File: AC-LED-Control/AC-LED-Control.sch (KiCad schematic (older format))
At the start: 1 part

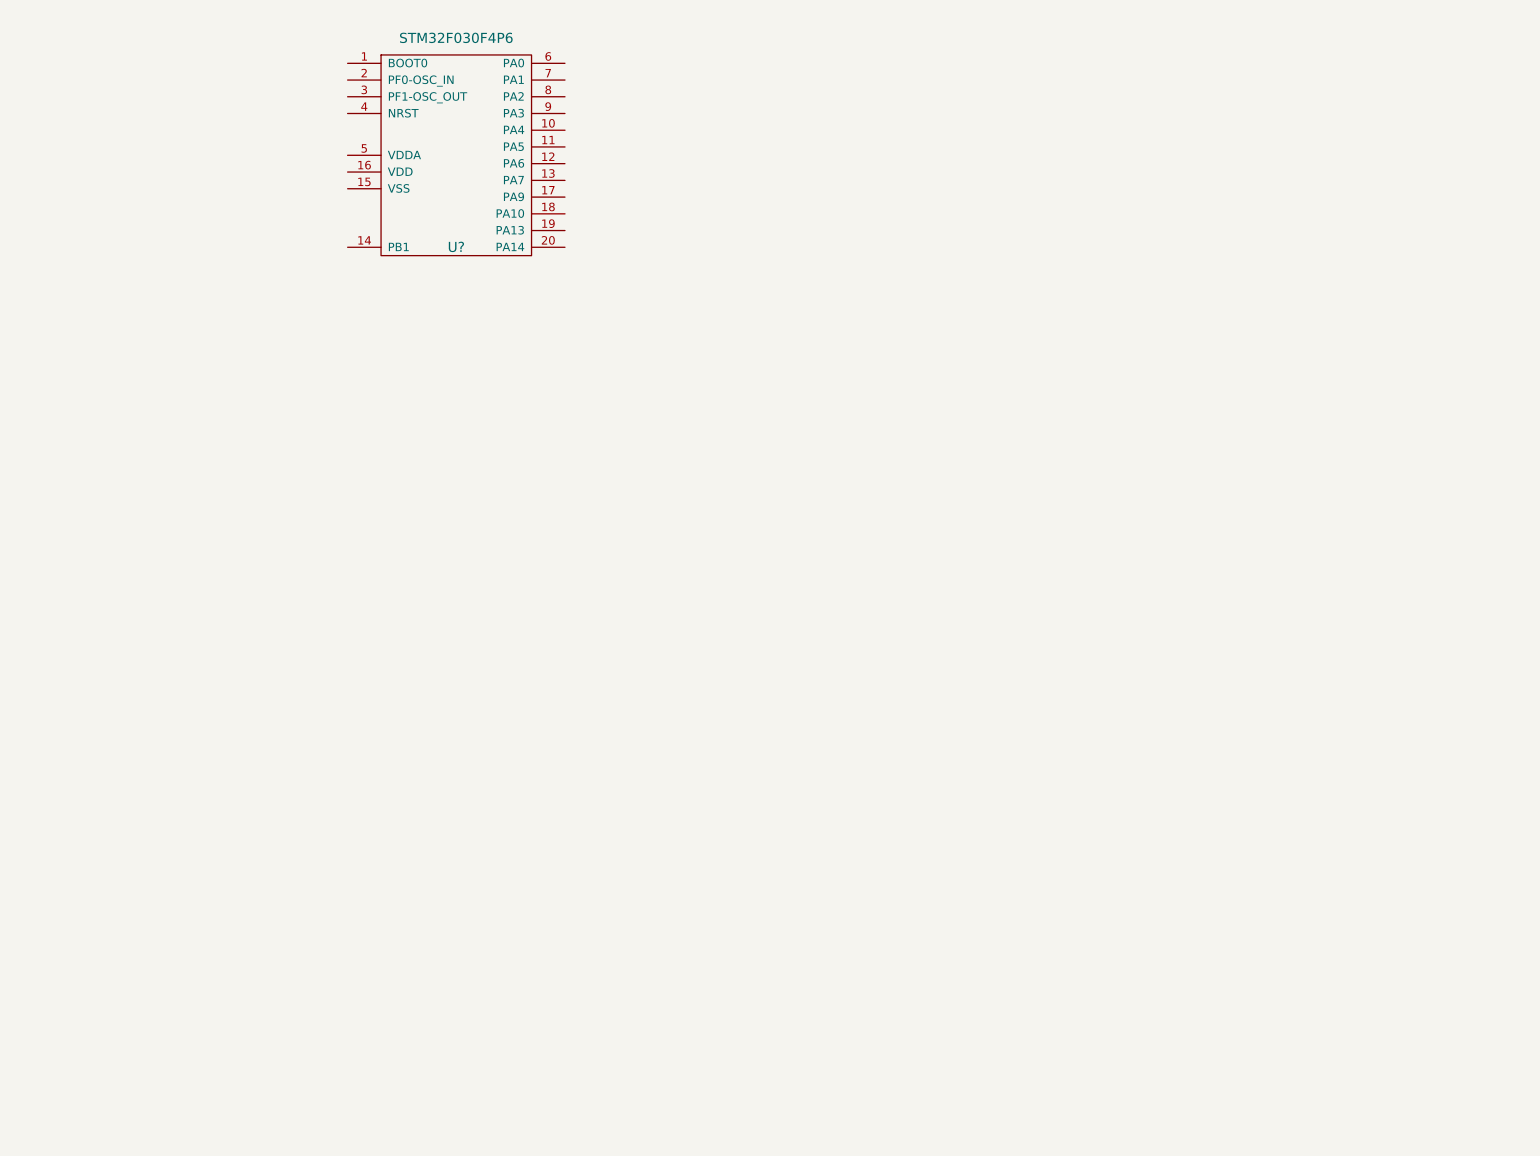
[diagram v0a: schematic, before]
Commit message: Added notes.md and started digital stuff.
- Added notes.md
- Added bypass caps to STM32
- Added I2C stuff
- Added 2 SN74HC595's and various nets
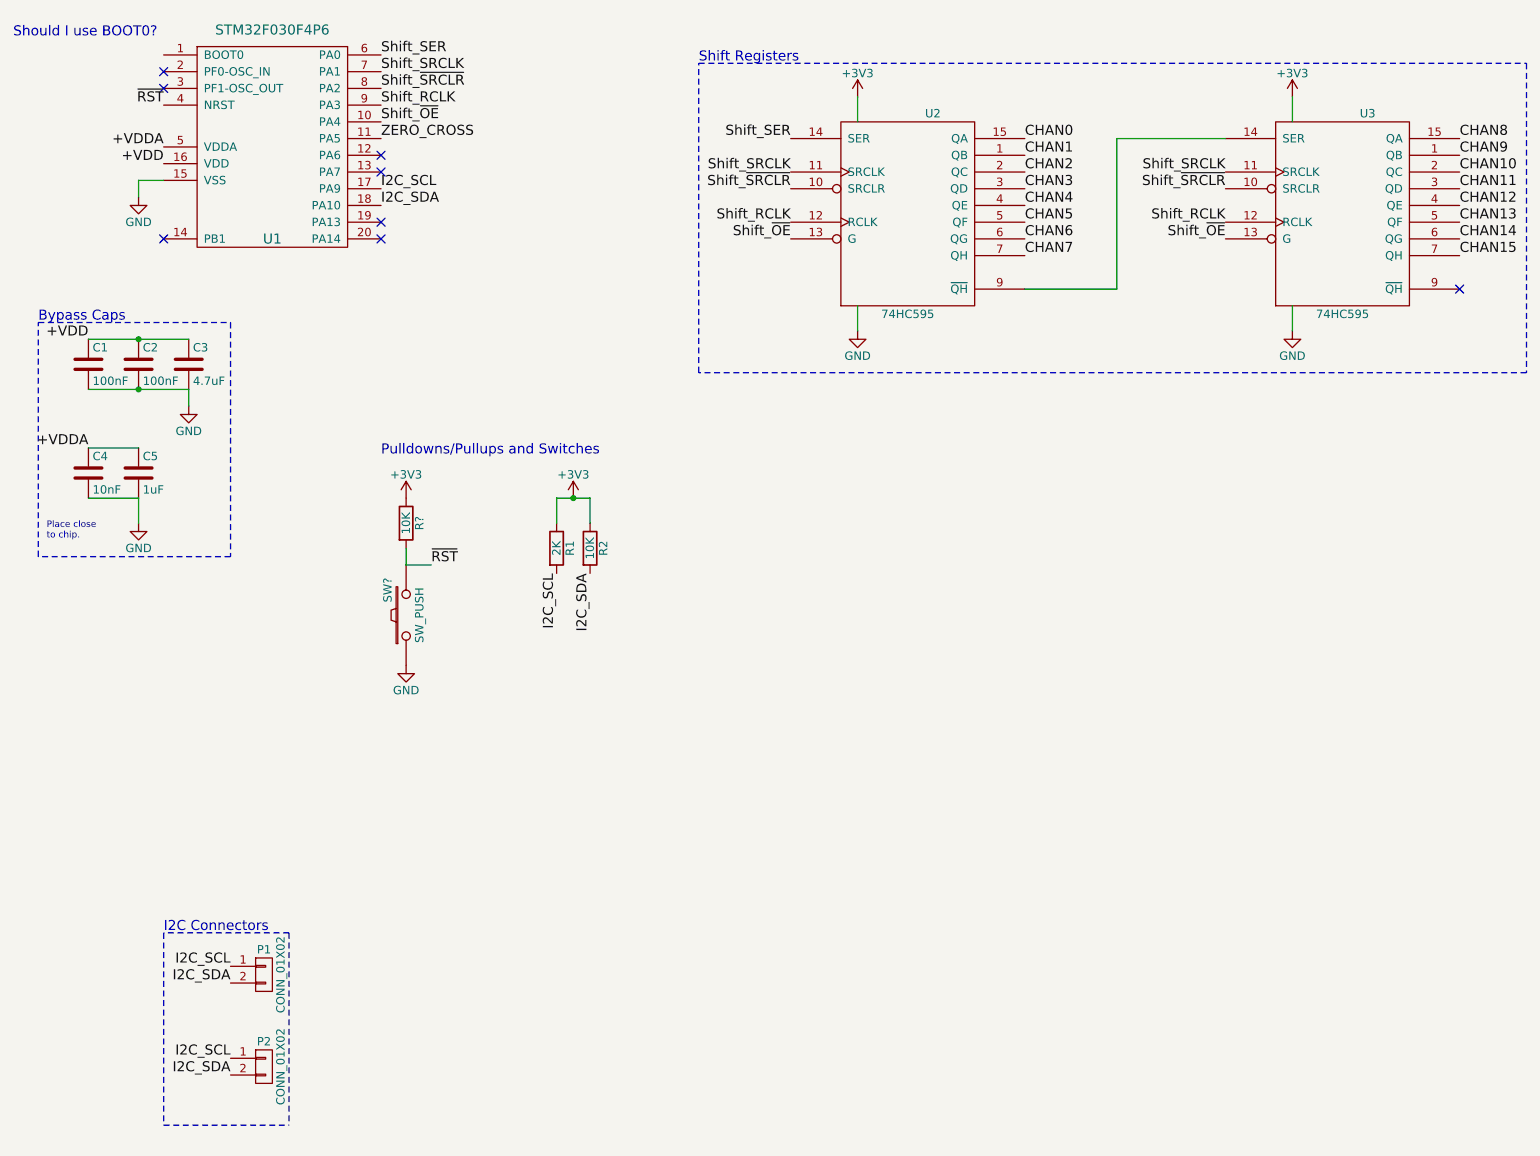
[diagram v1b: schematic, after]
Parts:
- added C1, C2: 100nF, symbol C
- added C3: 4.7uF, symbol C
- added C4: 10nF, symbol C
- added C5: 1uF, symbol C
- added P1, P2: CONN_01X02, symbol CONN_01X02
- added R1: 2K, symbol R
- added R2, R?: 10K, symbol R
- added SW?: SW_PUSH, symbol SW_PUSH
- added U2, U3: 74HC595, symbol 74HC595
- gave numbers to parts that had none: 1
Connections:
- net Shift_~OE: now reaches U1.10 (PA4)
- net Shift_~OE: now also U2.13 (G), U3.13 (G)
- net ZERO_CROSS: now reaches U1.11 (PA5)
- net GND: now reaches U1.15 (VSS)
- net GND: now also C1.2, C2.2, C3.2, C4.2, C5.2, SW?.1, U2.8 (GND), U3.8 (GND)
- net +VDD: now reaches U1.16 (VDD)
- net +VDD: now also C1.1, C2.1, C3.1
- net I2C_SCL: now reaches U1.17 (PA9)
- net I2C_SCL: now also P1.1 (P1), P2.1 (P1), R1.2
- net I2C_SDA: now reaches U1.18 (PA10)
- net I2C_SDA: now also P1.2 (P2), P2.2 (P2), R2.2
- net ~RST: now reaches U1.4 (NRST)
- net ~RST: now also R?.2, SW?.2
- net +VDDA: now reaches U1.5 (VDDA)
- net +VDDA: now also C4.1, C5.1
- net Shift_SER: now reaches U1.6 (PA0)
- net Shift_SER: now also U2.14 (SER)
- net Shift_SRCLK: now reaches U1.7 (PA1)
- net Shift_SRCLK: now also U2.11 (SRCLK), U3.11 (SRCLK)
- net Shift_~SRCLR: now reaches U1.8 (PA2)
- net Shift_~SRCLR: now also U2.10 (SRCLR), U3.10 (SRCLR)
- net Shift_RCLK: now reaches U1.9 (PA3)
- net Shift_RCLK: now also U2.12 (RCLK), U3.12 (RCLK)
- new net: U2.9 (~QH), U3.14 (SER)
- new net +3V3: R1.1, R2.1, R?.1, U2.16 (VCC), U3.16 (VCC)
- new net CHAN0: U2.15 (QA)
- new net CHAN1: U2.1 (QB)
- new net CHAN10: U3.2 (QC)
- new net CHAN11: U3.3 (QD)
- new net CHAN12: U3.4 (QE)
- new net CHAN13: U3.5 (QF)
- new net CHAN14: U3.6 (QG)
- new net CHAN15: U3.7 (QH)
- new net CHAN2: U2.2 (QC)
- new net CHAN3: U2.3 (QD)
- new net CHAN4: U2.4 (QE)
- new net CHAN5: U2.5 (QF)
- new net CHAN6: U2.6 (QG)
- new net CHAN7: U2.7 (QH)
- new net CHAN8: U3.15 (QA)
- new net CHAN9: U3.1 (QB)
- no-connect marks 0 -> 8
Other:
- note added: "Bypass Caps\n"
- note added: "I2C Connectors\n"
- note added: "Place close\nto chip."
- note added: "Pulldowns/Pullups and Switches"
- note added: "Shift Registers"
- note added: "Should I use BOOT0?"
- moved on the sheet: U1

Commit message: Pulled BOOT0 to GND
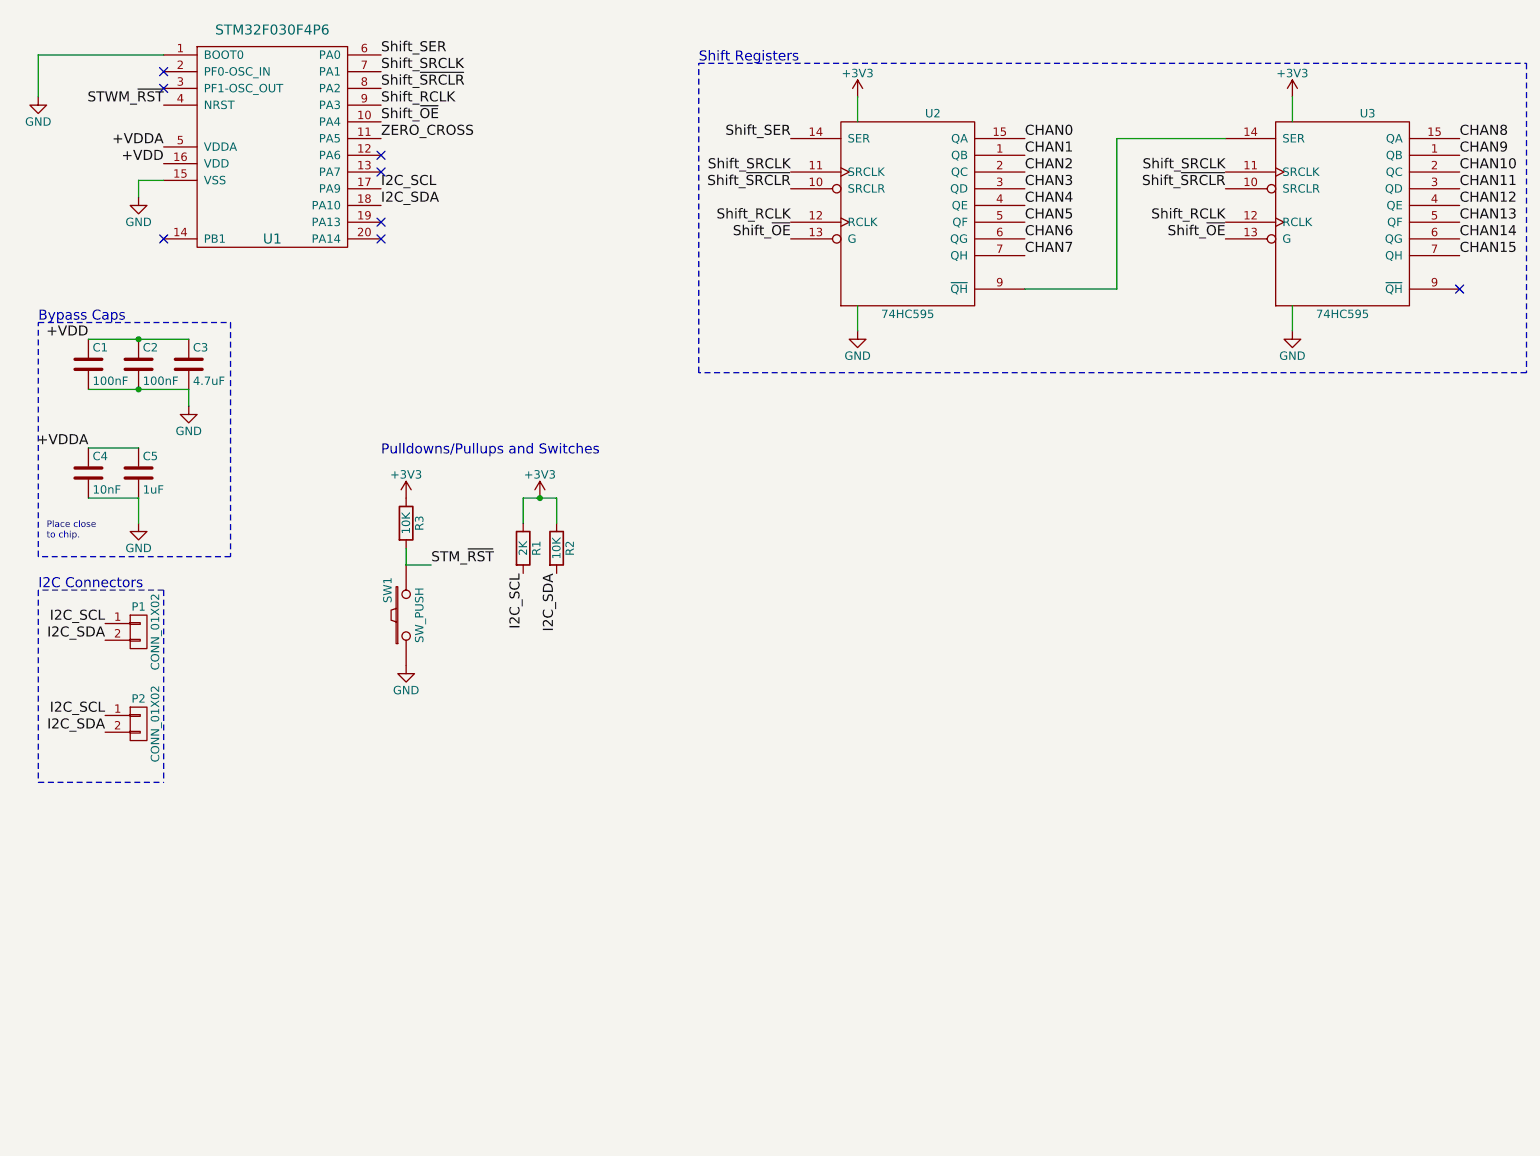
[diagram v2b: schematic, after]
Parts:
- gave numbers to parts that had none: 2
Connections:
- net GND: now also U1.1 (BOOT0)
- net ~RST renamed STM_~RST
- net STM_~RST: no longer U1.4 (NRST)
- new net STWM_~RST: U1.4 (NRST)
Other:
- note removed: "Should I use BOOT0?"
- moved on the sheet: P1, P2, R1, R2
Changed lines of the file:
@@
 L CONN_01X02 P1
 U 1 1 5B453C99
-P 2150 6500
-F 0 "P1" H 2150 6650 50  0000 C CNN
-F 1 "CONN_01X02" V 2250 6500 50  0000 C CNN
-F 2 "" H 2150 6500 50  0000 C CNN
-F 3 "" H 2150 6500 50  0000 C CNN
-	1    2150 6500
+P 1400 4450
+F 0 "P1" H 1400 4600 50  0000 C CNN
+F 1 "CONN_01X02" V 1500 4450 50  0000 C CNN
+F 2 "" H 1400 4450 50  0000 C CNN
+F 3 "" H 1400 4450 50  0000 C CNN
+	1    1400 4450
 	1    0    0    -1
 $EndComp
@@
 L CONN_01X02 P2
 U 1 1 5B453DC6
-P 2150 7050
-F 0 "P2" H 2150 7200 50  0000 C CNN
-F 1 "CONN_01X02" V 2250 7050 50  0000 C CNN
-F 2 "" H 2150 7050 50  0000 C CNN
-F 3 "" H 2150 7050 50  0000 C CNN
-	1    2150 7050
-	1    0    0    -1
-$EndComp
-Text Label 1950 6450 2    60   ~ 0
+P 1400 5000
+F 0 "P2" H 1400 5150 50  0000 C CNN
+F 1 "CONN_01X02" V 1500 5000 50  0000 C CNN
+F 2 "" H 1400 5000 50  0000 C CNN
+F 3 "" H 1400 5000 50  0000 C CNN
+	1    1400 5000
+	1    0    0    -1
+$EndComp
+Text Label 1200 4400 2    60   ~ 0
 I2C_SCL
-Text Label 1950 6550 2    60   ~ 0
+Text Label 1200 4500 2    60   ~ 0
 I2C_SDA
-Text Label 1950 7000 2    60   ~ 0
+Text Label 1200 4950 2    60   ~ 0
 I2C_SCL
-Text Label 1950 7100 2    60   ~ 0
+Text Label 1200 5050 2    60   ~ 0
 I2C_SDA
 Wire Notes Line
-	2300 6250 2300 7400
-Text Notes 1550 6250 0    60   ~ 0
+	1550 4200 1550 5350
+Text Notes 800  4200 0    60   ~ 0
 I2C Connectors\n
+Text Label 3700 4100 3    60   ~ 0
+I2C_SCL
 Text Label 3900 4100 3    60   ~ 0
-I2C_SCL
-Text Label 4100 4100 3    60   ~ 0
 I2C_SDA
 $Comp
 L R R1
 U 1 1 5B453F03
+P 3700 3950
+F 0 "R1" V 3780 3950 50  0000 C CNN
+F 1 "2K" V 3700 3950 50  0000 C CNN
+F 2 "" V 3630 3950 50  0000 C CNN
+F 3 "" H 3700 3950 50  0000 C CNN
+	1    3700 3950
+	1    0    0    -1
+$EndComp
+$Comp
+L R R2
+U 1 1 5B453F30
 P 3900 3950
-F 0 "R1" V 3980 3950 50  0000 C CNN
-F 1 "2K" V 3900 3950 50  0000 C CNN
+F 0 "R2" V 3980 3950 50  0000 C CNN
+F 1 "10K" V 3900 3950 50  0000 C CNN
 F 2 "" V 3830 3950 50  0000 C CNN
 F 3 "" H 3900 3950 50  0000 C CNN
@@
 $EndComp
 $Comp
-L R R2
-U 1 1 5B453F30
-P 4100 3950
-F 0 "R2" V 4180 3950 50  0000 C CNN
-F 1 "10K" V 4100 3950 50  0000 C CNN
-F 2 "" V 4030 3950 50  0000 C CNN
-F 3 "" H 4100 3950 50  0000 C CNN
-	1    4100 3950
-	1    0    0    -1
-$EndComp
-$Comp
-L +3V3 #PWR4
+L +3V3 #PWR01
 U 1 1 5B45401C
-P 4000 3650
-F 0 "#PWR4" H 4000 3500 50  0001 C CNN
-F 1 "+3V3" H 4000 3790 50  0000 C CNN
-F 2 "" H 4000 3650 50  0000 C CNN
-F 3 "" H 4000 3650 50  0000 C CNN
-	1    4000 3650
-	1    0    0    -1
-$EndComp
-Wire Wire Line
-	3900 3800 3900 3650
-Wire Wire Line
-	3900 3650 4100 3650
-Wire Wire Line
-	4100 3650 4100 3800
-Connection ~ 4000 3650
+P 3800 3650
+F 0 "#PWR01" H 3800 3500 50  0001 C CNN
+F 1 "+3V3" H 3800 3790 50  0000 C CNN
+F 2 "" H 3800 3650 50  0000 C CNN
+F 3 "" H 3800 3650 50  0000 C CNN
+	1    3800 3650
+	1    0    0    -1
+$EndComp
+Wire Wire Line
+	3700 3800 3700 3650
+Wire Wire Line
+	3700 3650 3900 3650
+Wire Wire Line
+	3900 3650 3900 3800
+Connection ~ 3800 3650
 Text Label 1550 1650 2    60   ~ 0
 +VDD
@@
 	1400 1750 1400 1850
 $Comp
-L GND #PWR1
+L GND #PWR02
 U 1 1 5B454DB5
 P 1400 1850
-F 0 "#PWR1" H 1400 1600 50  0001 C CNN
+F 0 "#PWR02" H 1400 1600 50  0001 C CNN
 F 1 "GND" H 1400 1700 50  0000 C CNN
 F 2 "" H 1400 1850 50  0000 C CNN
@@
 $EndComp
 $Comp
-L GND #PWR2
+L GND #PWR03
 U 1 1 5B454DF7
 P 1700 3100
-F 0 "#PWR2" H 1700 2850 50  0001 C CNN
+F 0 "#PWR03" H 1700 2850 50  0001 C CNN
 F 1 "GND" H 1700 2950 50  0000 C CNN
 F 2 "" H 1700 3100 50  0000 C CNN
@@
 $EndComp
 $Comp
-L GND #PWR3
+L GND #PWR04
 U 1 1 5B454F8F
 P 1400 3800
-F 0 "#PWR3" H 1400 3550 50  0001 C CNN
+F 0 "#PWR04" H 1400 3550 50  0001 C CNN
 F 1 "GND" H 1400 3650 50  0000 C CNN
 F 2 "" H 1400 3800 50  0000 C CNN
@@
 	8300 1400 8300 1250
 $Comp
-L +3V3 #PWR?
+L +3V3 #PWR05
 U 1 1 5B455E79
 P 8300 1250
-F 0 "#PWR?" H 8300 1100 50  0001 C CNN
+F 0 "#PWR05" H 8300 1100 50  0001 C CNN
 F 1 "+3V3" H 8300 1390 50  0000 C CNN
 F 2 "" H 8300 1250 50  0000 C CNN
@@
 	8300 2500 8300 2650
 $Comp
-L GND #PWR?
+L GND #PWR06
 U 1 1 5B455F67
 P 8300 2650
-F 0 "#PWR?" H 8300 2400 50  0001 C CNN
+F 0 "#PWR06" H 8300 2400 50  0001 C CNN
 F 1 "GND" H 8300 2500 50  0000 C CNN
 F 2 "" H 8300 2650 50  0000 C CNN
@@
 	5700 1400 5700 1250
 $Comp
-L +3V3 #PWR?
+L +3V3 #PWR07
 U 1 1 5B456028
 P 5700 1250
-F 0 "#PWR?" H 5700 1100 50  0001 C CNN
+F 0 "#PWR07" H 5700 1100 50  0001 C CNN
 F 1 "+3V3" H 5700 1390 50  0000 C CNN
 F 2 "" H 5700 1250 50  0000 C CNN
@@
 	5700 2500 5700 2650
 $Comp
-L GND #PWR?
+L GND #PWR08
 U 1 1 5B4560F7
 P 5700 2650
-F 0 "#PWR?" H 5700 2400 50  0001 C CNN
+F 0 "#PWR08" H 5700 2400 50  0001 C CNN
 F 1 "GND" H 5700 2500 50  0000 C CNN
 F 2 "" H 5700 2650 50  0000 C CNN
@@
 NoConn ~ 1550 1100
 NoConn ~ 1550 1200
-Text Notes 650  900  0    60   ~ 0
-Should I use BOOT0?
 Text Label 1550 1300 2    60   ~ 0
-~RST
+STWM_~RST
 Text Label 3150 4050 0    60   ~ 0
-~RST
+STM_~RST
 Wire Wire Line
 	3150 4050 3000 4050
@@
 	3000 4050 3000 3950
 $Comp
-L +3V3 #PWR?
+L +3V3 #PWR09
 U 1 1 5B4571F5
 P 3000 3650
-F 0 "#PWR?" H 3000 3500 50  0001 C CNN
+F 0 "#PWR09" H 3000 3500 50  0001 C CNN
 F 1 "+3V3" H 3000 3790 50  0000 C CNN
 F 2 "" H 3000 3650 50  0000 C CNN
@@
 $EndComp
 $Comp
-L R R?
+L R R3
 U 1 1 5B45725E
 P 3000 3800
-F 0 "R?" V 3080 3800 50  0000 C CNN
+F 0 "R3" V 3080 3800 50  0000 C CNN
 F 1 "10K" V 3000 3800 50  0000 C CNN
 F 2 "" V 2930 3800 50  0000 C CNN
@@
 Pulldowns/Pullups and Switches
 $Comp
-L SW_PUSH SW?
+L SW_PUSH SW1
 U 1 1 5B4574FB
 P 3000 4350
-F 0 "SW?" H 3150 4460 50  0000 C CNN
+F 0 "SW1" H 3150 4460 50  0000 C CNN
 F 1 "SW_PUSH" H 3000 4270 50  0000 C CNN
 F 2 "" H 3000 4350 50  0000 C CNN
@@
 $EndComp
 $Comp
-L GND #PWR?
+L GND #PWR010
 U 1 1 5B4575F8
 P 3000 4650
-F 0 "#PWR?" H 3000 4400 50  0001 C CNN
+F 0 "#PWR010" H 3000 4400 50  0001 C CNN
 F 1 "GND" H 3000 4500 50  0000 C CNN
 F 2 "" H 3000 4650 50  0000 C CNN
@@
 $EndComp
 Wire Notes Line
-	2300 6250 1550 6250
-Wire Notes Line
-	1550 6250 1550 7400
-Wire Notes Line
-	1550 7400 2300 7400
+	1550 4200 800  4200
+Wire Notes Line
+	800  4200 800  5350
+Wire Notes Line
+	800  5350 1550 5350
+Wire Wire Line
+	1550 1000 800  1000
+Wire Wire Line
+	800  1000 800  1250
+$Comp
+L GND #PWR011
+U 1 1 5B45876A
+P 800 1250
+F 0 "#PWR011" H 800 1000 50  0001 C CNN
+F 1 "GND" H 800 1100 50  0000 C CNN
+F 2 "" H 800 1250 50  0000 C CNN
+F 3 "" H 800 1250 50  0000 C CNN
+	1    800  1250
+	1    0    0    -1
+$EndComp
 $EndSCHEMATC
